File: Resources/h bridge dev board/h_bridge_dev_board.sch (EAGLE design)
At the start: 113 parts, among them IC1 74LS08N, IC2 74LS08N, IC3 74LS08N, IC4 7404N, IC5 74LS595N, IC6 74158N, IC7 LM358N, J1 J50MM, J2 J50MM, J25 J50MM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

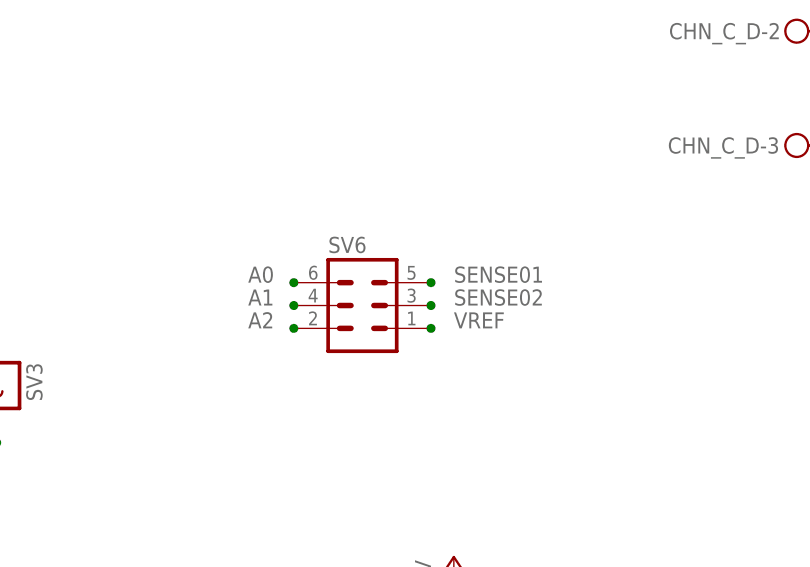
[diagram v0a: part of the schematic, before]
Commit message: prili board placement
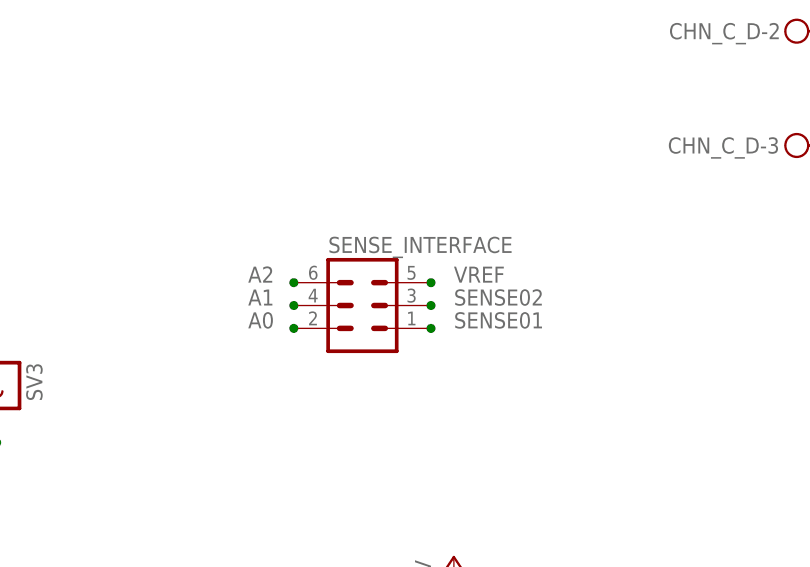
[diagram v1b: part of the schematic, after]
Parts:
- renumbered SV6 to SENSE_INTERFACE
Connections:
- net A0: now also SENSE_INTERFACE.2; no longer SENSE_INTERFACE.6
- net A2: now also SENSE_INTERFACE.6; no longer SENSE_INTERFACE.2
- net SENSE01: now also SENSE_INTERFACE.1; no longer SENSE_INTERFACE.5
- net VREF: now also SENSE_INTERFACE.5; no longer SENSE_INTERFACE.1
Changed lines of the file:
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@@
 <part name="SV4" library="con-lsta" deviceset="FE08-1" device=""/>
 <part name="SV5" library="con-lsta" deviceset="FE08-1" device=""/>
-<part name="SV6" library="con-lstb" deviceset="MA03-2" device=""/>
+<part name="SENSE_INTERFACE" library="con-lstb" deviceset="MA03-2" device=""/>
 <part name="R2" library="resistor" deviceset="R-US_" device="0207/12" value="3.3k"/>
 <part name="R3" library="resistor" deviceset="R-US_" device="0207/12" value="10k"/>
@@
 <instance part="SV4" gate="G$1" x="-292.1" y="-175.26" rot="R90"/>
 <instance part="SV5" gate="G$1" x="-261.62" y="-175.26" rot="R90"/>
-<instance part="SV6" gate="1" x="-200.66" y="-73.66"/>
+<instance part="SENSE_INTERFACE" gate="1" x="-200.66" y="-73.66"/>
 <instance part="R2" gate="G$1" x="-190.5" y="-109.22" rot="R90"/>
 <instance part="R3" gate="G$1" x="-190.5" y="-124.46" rot="R90"/>
@@
 </segment>
 <segment>
-<pinref part="SV6" gate="1" pin="5"/>
-<junction x="-193.04" y="-71.12"/>
-<label x="-190.5" y="-71.12" size="1.778" layer="95"/>
+<pinref part="SENSE_INTERFACE" gate="1" pin="1"/>
+<junction x="-193.04" y="-76.2"/>
+<label x="-190.5" y="-76.2" size="1.778" layer="95"/>
 </segment>
 </net>
@@
 </segment>
 <segment>
-<pinref part="SV6" gate="1" pin="3"/>
+<pinref part="SENSE_INTERFACE" gate="1" pin="3"/>
 <junction x="-193.04" y="-73.66"/>
 <label x="-190.5" y="-73.66" size="1.778" layer="95"/>
@@
 <net name="VREF" class="0">
 <segment>
-<pinref part="SV6" gate="1" pin="1"/>
-<junction x="-193.04" y="-76.2"/>
-<label x="-190.5" y="-76.2" size="1.778" layer="95"/>
-</segment>
-<segment>
 <pinref part="VREF" gate="G$1" pin="S"/>
 <junction x="-172.72" y="-124.46"/>
 <label x="-170.18" y="-124.46" size="1.778" layer="95"/>
 </segment>
+<segment>
+<pinref part="SENSE_INTERFACE" gate="1" pin="5"/>
+<junction x="-193.04" y="-71.12"/>
+<label x="-190.5" y="-71.12" size="1.778" layer="95"/>
+</segment>
 </net>
 <net name="D9" class="0">
@@
 <net name="A2" class="0">
 <segment>
-<pinref part="SV6" gate="1" pin="2"/>
-<junction x="-208.28" y="-76.2"/>
-<label x="-213.36" y="-76.2" size="1.778" layer="95"/>
-</segment>
-<segment>
 <pinref part="SV4" gate="G$1" pin="3"/>
 <junction x="-289.56" y="-167.64"/>
@@
 <label x="-266.7" y="-149.86" size="1.778" layer="95" rot="R270"/>
 </segment>
+<segment>
+<pinref part="SENSE_INTERFACE" gate="1" pin="6"/>
+<junction x="-208.28" y="-71.12"/>
+<label x="-213.36" y="-71.12" size="1.778" layer="95"/>
+</segment>
 </net>
 <net name="A1" class="0">
 <segment>
-<pinref part="SV6" gate="1" pin="4"/>
+<pinref part="SENSE_INTERFACE" gate="1" pin="4"/>
 <junction x="-208.28" y="-73.66"/>
 <label x="-213.36" y="-73.66" size="1.778" layer="95"/>
@@
 <net name="A0" class="0">
 <segment>
-<pinref part="SV6" gate="1" pin="6"/>
-<junction x="-208.28" y="-71.12"/>
-<label x="-213.36" y="-71.12" size="1.778" layer="95"/>
-</segment>
-<segment>
 <pinref part="SV4" gate="G$1" pin="5"/>
 <junction x="-294.64" y="-167.64"/>
@@
 <label x="-271.78" y="-149.86" size="1.778" layer="95" rot="R270"/>
 </segment>
-</net>
+<segment>
+<pinref part="SENSE_INTERFACE" gate="1" pin="2"/>
+<junction x="-208.28" y="-76.2"/>
+<label x="-213.36" y="-76.2" size="1.778" layer="95"/>
+</segment>
+</net>

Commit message: microstep works with l298 at 20KHz. ipdate schematic with active RC low pass filters
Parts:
- added C3, C4: 100n, rcl:C-EU050-030X075
- added IC8: LM358N, linear:LM358N
- added R1, R12: 2.2k, rcl:R-EU_0207/10
- CAP_AH, CAP_AL, CAP_BH, CAP_BL, CAP_CH, CAP_CL, CAP_DH: value J15MM -> (none); device jumper:J15MM -> rcl:C-EU050-030X075
- CAP_DL: device jumper:J15MM -> rcl:C-EU050-030X075
- DB_AH, DB_AL, DB_BH, DB_BL, DB_CH, DB_CL, DB_DH, DB_DL, DF_AH, DF_AL, DF_BH, DF_BL, DF_CH, DF_CL, DF_DH, DF_DL, DR_AH, DR_AL, DR_BH, DR_BL, DR_CH, DR_CL, DR_DH, DR_DL: value J15MM -> (none); device jumper:J15MM -> diode:DIODE-DO27-15
- R10, R11, R4, R5, R6, R7, R8, R9: device resistor:R-US_0207/10 -> rcl:R-EU_0207/10
- R2, R3: device resistor:R-US_0207/12 -> rcl:R-EU_0207/10
- RES_BASE_AH, RES_BASE_AL, RES_BASE_BH, RES_BASE_BL, RES_BASE_CH, RES_BASE_CL, RES_BASE_DH: value J15MM -> (none); device jumper:J15MM -> rcl:R-EU_0207/10
- RES_BASE_DL: device jumper:J15MM -> rcl:R-EU_0207/10
- R_F_AB, R_F_CD, R_G_AB, R_G_CD: value J10MM -> (none); device jumper:J10MM -> rcl:R-EU_0207/10
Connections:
- removed net N$10: CAP_AL.1, RES_BASE_AL.2
- removed net N$22: CAP_CH.1, RES_BASE_CH.1
- removed net N$23: CAP_CL.1, RES_BASE_CL.2
- removed net N$24: CAP_BH.2, RES_BASE_BH.1
- removed net N$26: CAP_BL.2, RES_BASE_BL.1
- removed net N$28: CAP_DH.2, RES_BASE_DH.1
- removed net N$7: CAP_DL.1, DB_DL.1, DF_DL.1, DR_DL.1
- removed net N$9: CAP_AH.1, RES_BASE_AH.2
- new net N$46: C3.1, IC8B.+IN, R1.1
- new net N$47: C4.1, IC8A.+IN, R12.1
- new net SENSE01_FILTER: IC8B.-IN, IC8B.OUT, SENSE_INTERFACE.1
- new net SENSE02_FILTER: IC8A.-IN, IC8A.OUT, SENSE_INTERFACE.3
- net +5V: now also IC8P.V+
- net AH: now also DB_AH.C, DR_AH.A; no longer DB_AH.2, DR_AH.2
- net AL: now also DB_AL.C, DR_AL.A; no longer DB_AL.2, DR_AL.2
- net BH: now also DB_BH.C, DR_BH.A; no longer DB_BH.2, DR_BH.2
- net BL: now also DB_BL.C, DR_BL.A; no longer DB_BL.2, DR_BL.2
- net CH: now also DB_CH.C, DR_CH.A; no longer DB_CH.2, DR_CH.2
- net CL: now also DB_CL.C, DR_CL.A; no longer DB_CL.2, DR_CL.2
- net DH: now also DB_DH.C, DR_DH.A; no longer DB_DH.2, DR_DH.2
- net DL: now also DB_DL.C, DR_DL.A; no longer DB_DL.2, DR_DL.2
- net GND: now also C3.2, C4.2, IC8P.V-
- net N$19: now also DB_CL.A, DF_CL.A, DR_CL.C, RES_BASE_CL.2; no longer DB_CL.1, DF_CL.1, DR_CL.1
- net N$20: now also DB_AH.A, DF_AH.A, DR_AH.C, RES_BASE_AH.2; no longer DB_AH.1, DF_AH.1, DR_AH.1
- net N$21: now also DB_BH.A, DF_BH.A, DR_BH.C, RES_BASE_BH.1; no longer DB_BH.1, DF_BH.1, DR_BH.1
- net N$29: now also CAP_DL.1, DB_DL.A, DF_DL.A, DR_DL.C; no longer CAP_DL.2
- net N$34: now also CAP_DL.2
- net N$35: now also CAP_BH.2
- net N$36: now also CAP_BL.2
- net N$37: now also CAP_DH.2
- net N$38: now also CAP_CL.1
- net N$39: now also CAP_CH.1
- net N$4: now also DB_AL.A, DF_AL.A, DR_AL.C, RES_BASE_AL.2; no longer DB_AL.1, DF_AL.1, DR_AL.1
- net N$42: now also CAP_AL.1
- net N$43: now also CAP_AH.1
- net N$5: now also DB_CH.A, DF_CH.A, DR_CH.C, RES_BASE_CH.1; no longer DB_CH.1, DF_CH.1, DR_CH.1
- net N$6: now also DB_BL.A, DF_BL.A, DR_BL.C, RES_BASE_BL.1; no longer DB_BL.1, DF_BL.1, DR_BL.1
- net N$8: now also DB_DH.A, DF_DH.A, DR_DH.C, RES_BASE_DH.1; no longer DB_DH.1, DF_DH.1, DR_DH.1
- net OUT_A: now also DF_AL.C; no longer DF_AL.2
- net OUT_B: now also DF_BL.C; no longer DF_BL.2
- net OUT_C: now also DF_CL.C; no longer DF_CL.2
- net OUT_D: now also DF_DL.C; no longer DF_DL.2
- net SENSE01: now also R1.2; no longer SENSE_INTERFACE.1
- net SENSE02: now also R12.2; no longer SENSE_INTERFACE.3
- net VCC: now also DF_AH.C, DF_BH.C, DF_CH.C, DF_DH.C; no longer DF_AH.2, DF_BH.2, DF_CH.2, DF_DH.2
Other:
- moved on the sheet: OK1, OK2, OK3, OK4, OK5, OK6, OK7, OK8, SENSE_INTERFACE, SW_DPDT, VREF
